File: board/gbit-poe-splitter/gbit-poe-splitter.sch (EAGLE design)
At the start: 51 parts, among them IC1 LM2596HVS, U1 TPS2379DDA

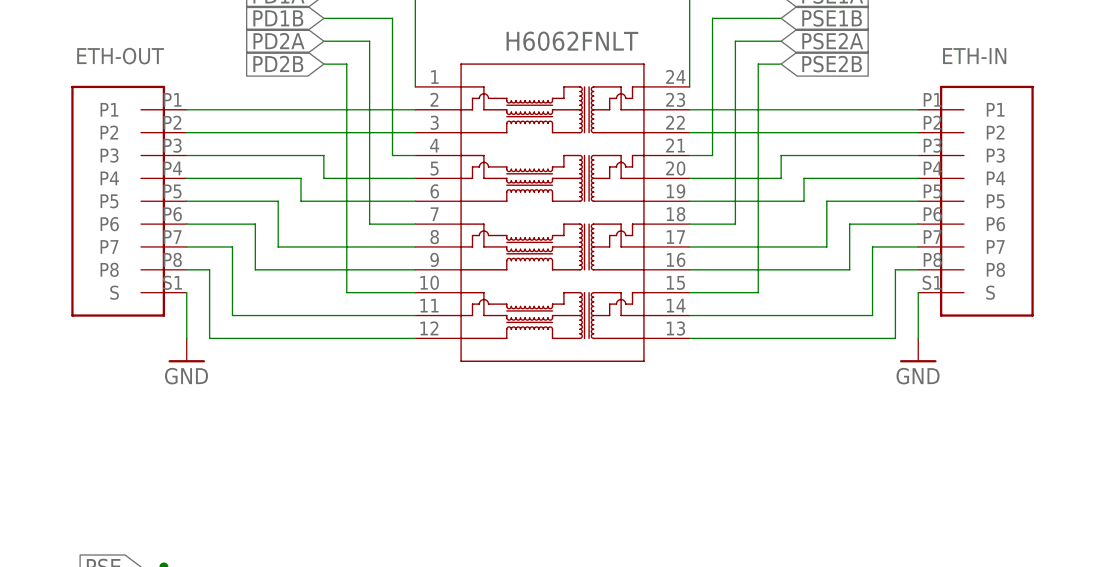
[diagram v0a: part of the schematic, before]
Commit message: Began the routing process
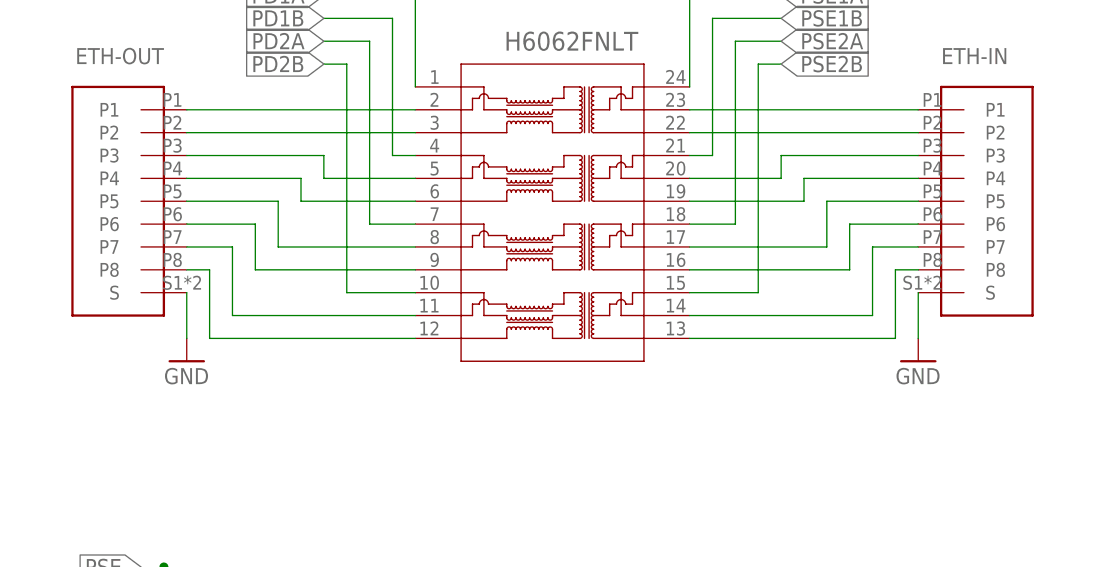
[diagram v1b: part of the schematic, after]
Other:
- moved on the sheet: ETH-IN, ETH-OUT

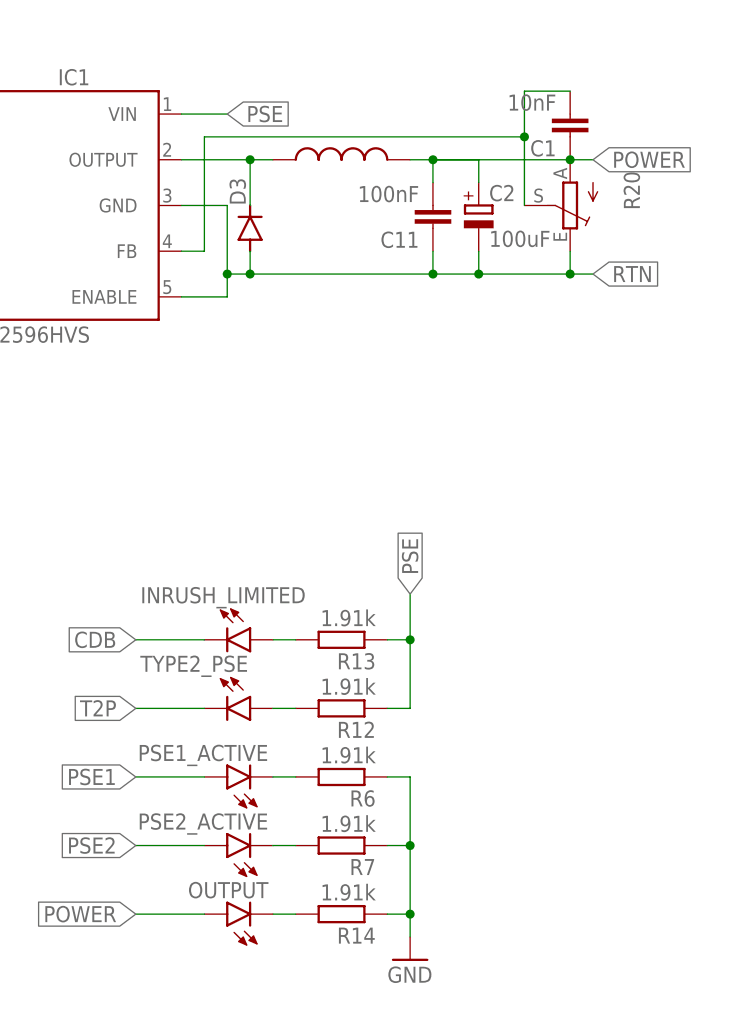
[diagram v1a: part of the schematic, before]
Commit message: Completed board layout
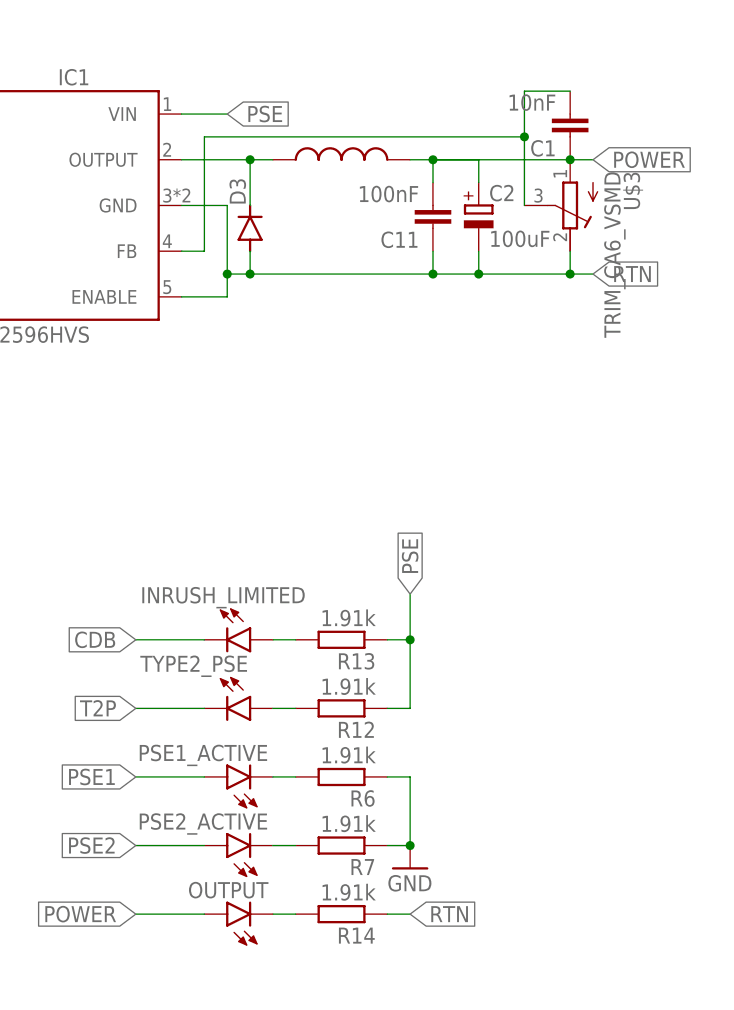
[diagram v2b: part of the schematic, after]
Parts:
- removed R20: (no value), pot:TRIM_EU-S64W
- added U$3: TRIM_CA6_VSMD, TRIM_CA6_VSMD:TRIM_CA6_VSMD
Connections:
- net GND: no longer R14.1
- net N$37: now also U$3.S; no longer R20.S
- net POWER: now also U$3.A; no longer R20.A
- net RTN: now also R14.1, U$3.E; no longer R20.E
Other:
- moved on the sheet: IC1
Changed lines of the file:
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@@
 <part name="D3" library="diode" library_urn="urn:adsk.eagle:library:210" deviceset="DIODE-" device="DO-214AC" package3d_urn="urn:adsk.eagle:package:43416/2"/>
 <part name="U$2" library="smd-inductors" deviceset="INDUCTOR-SMD" device="7070"/>
-<part name="R20" library="pot" library_urn="urn:adsk.eagle:library:331" deviceset="TRIM_EU-" device="S64W" package3d_urn="urn:adsk.eagle:package:22708/1"/>
 <part name="C1" library="rcl" library_urn="urn:adsk.eagle:library:334" deviceset="C-EU" device="C0603K" package3d_urn="urn:adsk.eagle:package:23680/2" value="10nF"/>
+<part name="U$3" library="TRIM_CA6_VSMD" deviceset="TRIM_CA6_VSMD" device=""/>
 </parts>
 <sheets>
@@
 <attribute name="VALUE" x="87.63" y="8.382" size="1.778" layer="96" rot="R180"/>
 </instance>
-<instance part="GND5" gate="1" x="91.44" y="-7.62" smashed="yes" grouprefs="STATUS_LEDS">
-<attribute name="VALUE" x="88.9" y="-10.16" size="1.778" layer="96"/>
+<instance part="GND5" gate="1" x="91.44" y="2.54" smashed="yes" grouprefs="STATUS_LEDS">
+<attribute name="VALUE" x="88.9" y="0" size="1.778" layer="96"/>
 </instance>
 <instance part="R12" gate="G$1" x="83.82" y="20.32" smashed="yes" rot="R180" grouprefs="STATUS_LEDS">
@@
 </instance>
 <instance part="U$2" gate="G$1" x="83.82" y="81.28" smashed="yes" grouprefs="VOLTAGE_REG"/>
-<instance part="R20" gate="1" x="109.22" y="76.2" smashed="yes" rot="R180" grouprefs="VOLTAGE_REG">
-<attribute name="NAME" x="115.189" y="80.01" size="1.778" layer="95" rot="R270"/>
-<attribute name="VALUE" x="113.03" y="80.01" size="1.778" layer="96" rot="R270"/>
-</instance>
 <instance part="C1" gate="G$1" x="109.22" y="83.82" smashed="yes" rot="R180" grouprefs="VOLTAGE_REG">
 <attribute name="NAME" x="107.696" y="83.439" size="1.778" layer="95" rot="R180"/>
 <attribute name="VALUE" x="107.696" y="88.519" size="1.778" layer="96" rot="R180"/>
+</instance>
+<instance part="U$3" gate="G$1" x="109.22" y="76.2" smashed="yes" rot="R180">
+<attribute name="NAME" x="115.189" y="80.01" size="1.778" layer="95" rot="R270"/>
+<attribute name="VALUE" x="113.03" y="80.01" size="1.778" layer="96" rot="R270"/>
 </instance>
 </instances>
@@
 <pinref part="R7" gate="G$1" pin="1"/>
 <wire x1="91.44" y1="5.08" x2="88.9" y2="5.08" width="0.1524" layer="91" grouprefs="STATUS_LEDS"/>
-<wire x1="91.44" y1="5.08" x2="91.44" y2="-2.54" width="0.1524" layer="91" grouprefs="STATUS_LEDS"/>
 <junction x="91.44" y="5.08" grouprefs="STATUS_LEDS"/>
 <pinref part="GND5" gate="1" pin="GND"/>
-<pinref part="R14" gate="G$1" pin="1"/>
-<wire x1="91.44" y1="-2.54" x2="91.44" y2="-5.08" width="0.1524" layer="91" grouprefs="STATUS_LEDS"/>
-<wire x1="88.9" y1="-2.54" x2="91.44" y2="-2.54" width="0.1524" layer="91" grouprefs="STATUS_LEDS"/>
-<junction x="91.44" y="-2.54" grouprefs="STATUS_LEDS"/>
 </segment>
 <segment>
@@
 <label x="111.76" y="81.28" size="1.778" layer="95" xref="yes" grouprefs="VOLTAGE_REG"/>
 <pinref part="U$2" gate="G$1" pin="2"/>
-<pinref part="R20" gate="1" pin="A"/>
 <wire x1="109.22" y1="81.28" x2="111.76" y2="81.28" width="0.1524" layer="91" grouprefs="VOLTAGE_REG"/>
 <junction x="109.22" y="81.28" grouprefs="VOLTAGE_REG"/>
 <pinref part="C1" gate="G$1" pin="1"/>
+<pinref part="U$3" gate="G$1" pin="A"/>
 </segment>
 </net>
@@
 <wire x1="71.12" y1="66.04" x2="71.12" y2="68.58" width="0.1524" layer="91" grouprefs="VOLTAGE_REG"/>
 <junction x="71.12" y="68.58" grouprefs="VOLTAGE_REG"/>
-<pinref part="R20" gate="1" pin="E"/>
 <wire x1="109.22" y1="71.12" x2="109.22" y2="68.58" width="0.1524" layer="91" grouprefs="VOLTAGE_REG"/>
 <junction x="109.22" y="68.58" grouprefs="VOLTAGE_REG"/>
+<pinref part="U$3" gate="G$1" pin="E"/>
+</segment>
+<segment>
+<pinref part="R14" gate="G$1" pin="1"/>
+<wire x1="88.9" y1="-2.54" x2="91.44" y2="-2.54" width="0.1524" layer="91"/>
+<label x="91.44" y="-2.54" size="1.778" layer="95" xref="yes"/>
 </segment>
 </net>
@@
 <wire x1="66.04" y1="71.12" x2="68.58" y2="71.12" width="0.1524" layer="91" grouprefs="VOLTAGE_REG"/>
 <wire x1="68.58" y1="71.12" x2="68.58" y2="83.82" width="0.1524" layer="91" grouprefs="VOLTAGE_REG"/>
-<pinref part="R20" gate="1" pin="S"/>
 <wire x1="104.14" y1="76.2" x2="104.14" y2="83.82" width="0.1524" layer="91" grouprefs="VOLTAGE_REG"/>
 <wire x1="104.14" y1="83.82" x2="68.58" y2="83.82" width="0.1524" layer="91" grouprefs="VOLTAGE_REG"/>
@@
 <wire x1="104.14" y1="88.9" x2="104.14" y2="83.82" width="0.1524" layer="91" grouprefs="VOLTAGE_REG"/>
 <junction x="104.14" y="83.82" grouprefs="VOLTAGE_REG"/>
-</segment>
-</net>
+<pinref part="U$3" gate="G$1" pin="S"/>
+</segment>
+</net>

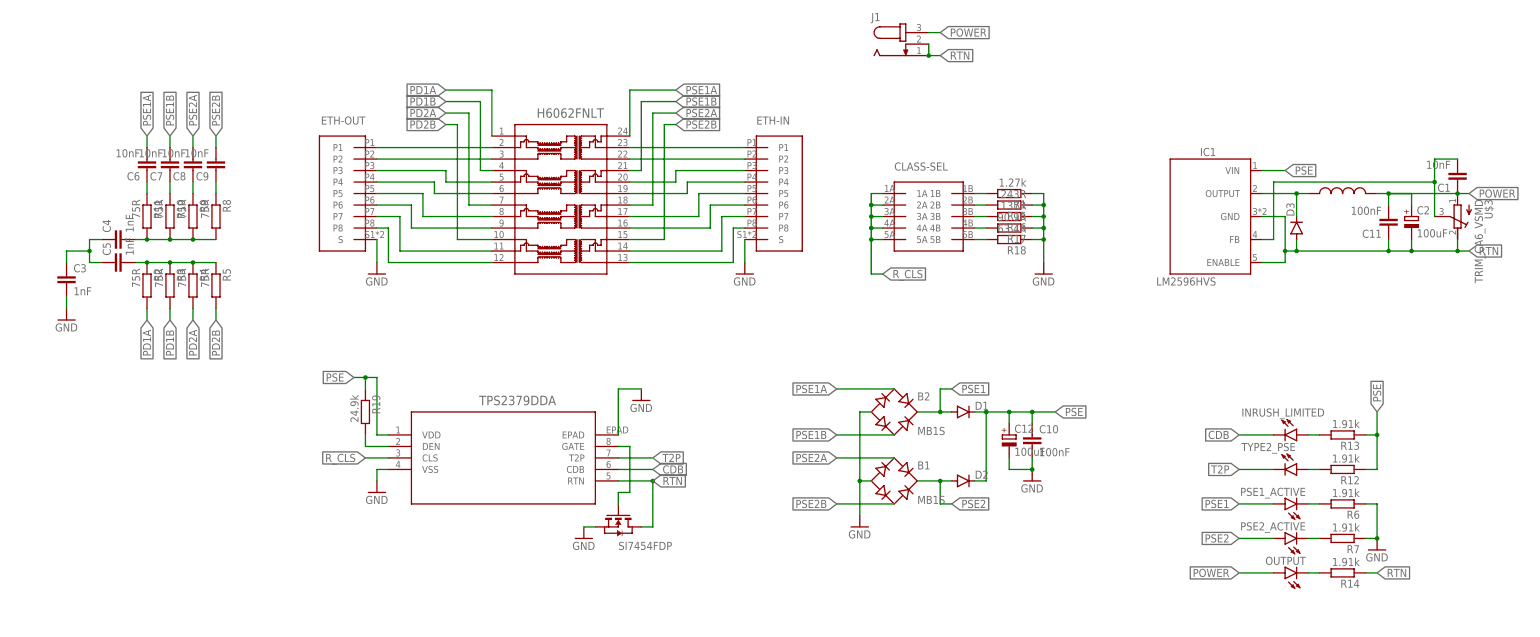
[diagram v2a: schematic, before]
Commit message: Fixed jack orientation, font and keepouts
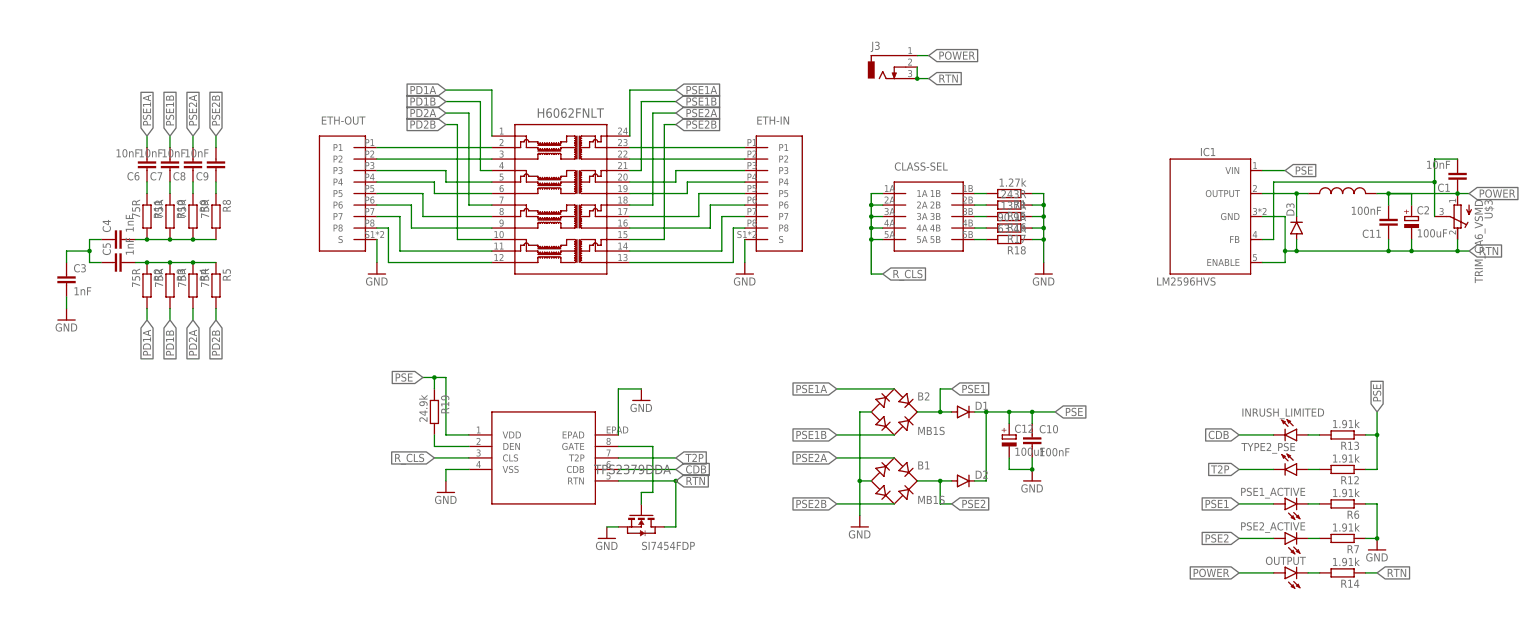
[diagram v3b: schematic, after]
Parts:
- removed J1: (no value), con-jack:JACK-PLUG1
- added J3: (no value), con-jack:DCJ0303
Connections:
- net POWER: now also J3.1; no longer J1.3
- net RTN: now also J3.2, J3.3; no longer J1.1, J1.2
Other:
- moved on the sheet: R19

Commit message: Fixed horrible ethernet pin swap
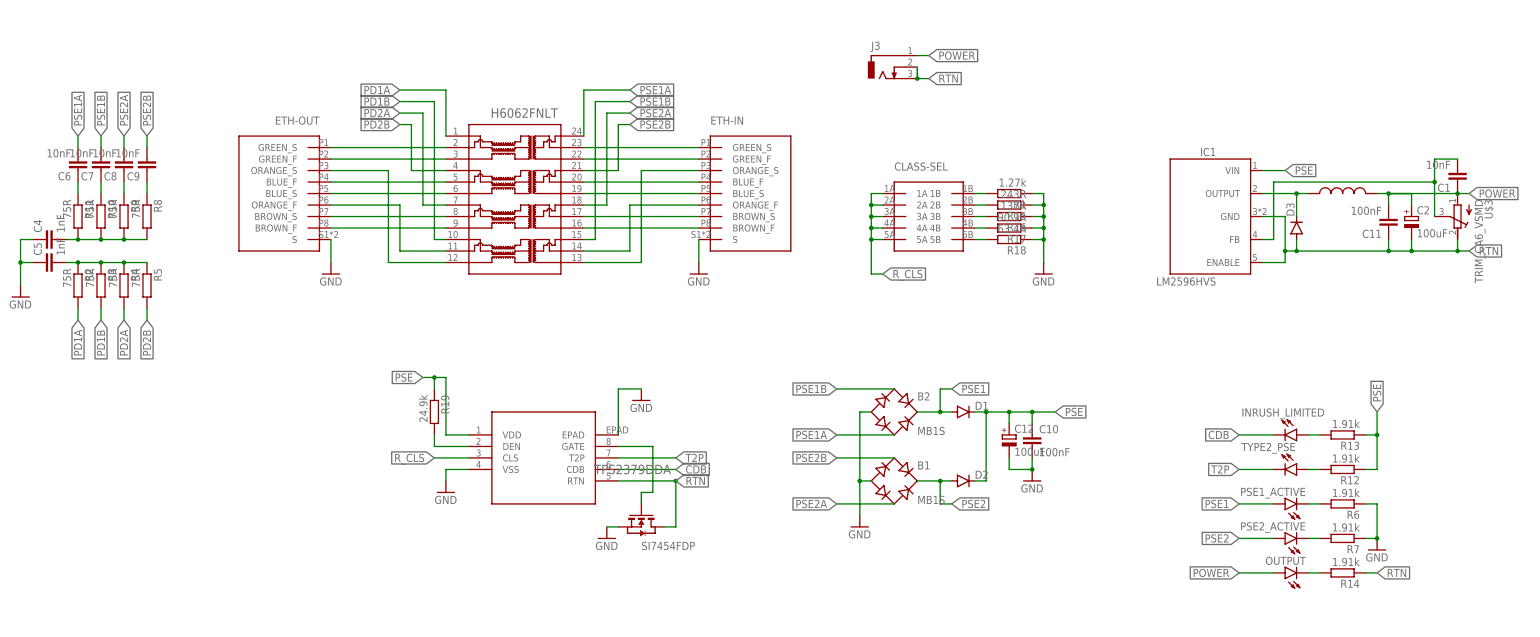
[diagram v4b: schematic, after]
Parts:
- removed C3: 1nF, rcl:C-EUC0603K
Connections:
- removed net N$17: C3.1, C4.1, C5.1
- net GND: now also C4.1, C5.1; no longer C3.2
- net N$1: now also ETH-OUT.GREEN_S; no longer ETH-OUT.P1
- net N$10: now also ETH-IN.BLUE_F, XMER1.20; no longer ETH-IN.P7, XMER1.14
- net N$11: now also ETH-IN.BROWN_F; no longer ETH-IN.P6
- net N$12: now also ETH-IN.BLUE_S, XMER1.19; no longer ETH-IN.P5, XMER1.17
- net N$13: now also ETH-IN.ORANGE_F, XMER1.14; no longer ETH-IN.P4, XMER1.19
- net N$14: now also ETH-IN.ORANGE_S, XMER1.13; no longer ETH-IN.P3, XMER1.20
- net N$15: now also ETH-IN.GREEN_F; no longer ETH-IN.P2
- net N$16: now also ETH-IN.GREEN_S; no longer ETH-IN.P1
- net N$2: now also ETH-OUT.GREEN_F; no longer ETH-OUT.P2
- net N$3: now also ETH-OUT.ORANGE_S, XMER1.12; no longer ETH-OUT.P3, XMER1.5
- net N$4: now also ETH-OUT.BLUE_F, XMER1.5; no longer ETH-OUT.P4, XMER1.6
- net N$5: now also ETH-OUT.BLUE_S, XMER1.6; no longer ETH-OUT.P5, XMER1.8
- net N$6: now also ETH-OUT.ORANGE_F, XMER1.11; no longer ETH-OUT.P6, XMER1.9
- net N$7: now also ETH-OUT.BROWN_S, XMER1.8; no longer ETH-OUT.P7, XMER1.11
- net N$8: now also ETH-OUT.BROWN_F, XMER1.9; no longer ETH-OUT.P8, XMER1.12
- net N$9: now also ETH-IN.BROWN_S, XMER1.17; no longer ETH-IN.P8, XMER1.13
- net PD1B: now also XMER1.10; no longer XMER1.4
- net PD2B: now also XMER1.4; no longer XMER1.10
- net PSE1A: now also B2.AC2; no longer B2.AC1
- net PSE1B: now also B2.AC1, XMER1.15; no longer B2.AC2, XMER1.21
- net PSE2A: now also B1.AC2; no longer B1.AC1
- net PSE2B: now also B1.AC1, XMER1.21; no longer B1.AC2, XMER1.15
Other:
- moved on the sheet: C4, C5, C6, C7, C8, C9, ETH-IN, ETH-OUT, R10, R11, R2, R3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
